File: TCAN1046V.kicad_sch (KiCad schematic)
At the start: 5 parts, among them U2 TCAN1051VDRBRQ1

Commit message: OBC: Continue PCB lauout
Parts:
- removed U2: TCAN1051VDRBRQ1, TCAN1051V:DRB8_TEX, symbol TCAN1051V:TCAN1051VDRBRQ1
- added U3: TCAN1046AVDYYRQ1, TCAN1046AV:SOT23_DYY_TEX, symbol TCAN1046AVDYYRQ1:TCAN1046AVDYYRQ1
- renumbered C3 to C4, C4 to C5, C5 to C6, C6 to C7
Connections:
- net GND: now also U3.2 (GND1), U3.5 (GND2)
- net VCC: now also U3.3 (VCC)
- net VIO: now also U3.11 (VIO)
- new net CANH1: U3.13 (CANH1)
- new net CANH2: U3.10 (CANH2)
- new net CANL1: U3.12 (CANL1)
- new net CANL2: U3.9 (CANL2)
- new net RXD1: U3.4 (RXD1)
- new net RXD2: U3.7 (RXD2)
- new net STB1: U3.14 (STB1)
- new net STB2: U3.8 (STB2/NSTB2)
- new net TXD1: U3.1 (TXD1)
- new net TXD2: U3.6 (TXD2)
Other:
- moved on the sheet: C4, C5, C6, C7

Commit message: Layout confirmed, PCBs ordered
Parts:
- C4, C6: DigiKey Part Number (none) -> 720-GA0805Y472KXBBC31GCT-ND
- C5, C7: DigiKey Part Number (none) -> 720-GA0805Y104JXABT31GCT-ND
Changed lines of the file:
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@@
 			)
 		)
-		(property "Datasheet" "https://www.ti.com/lit/gpn/tcan1046av-q1"
+		(property "Datasheet" ""
 			(at 186.69 128.27 0)
 			(effects
@@
 			)
 		)
+		(property "DigiKey Part Number" "720-GA0805Y104JXABT31GCT-ND"
+			(at 259.08 139.7 0)
+			(effects
+				(font
+					(size 1.27 1.27)
+				)
+				(hide yes)
+			)
+		)
 		(pin "2"
 		)
@@
 			)
 		)
+		(property "DigiKey Part Number" "720-GA0805Y472KXBBC31GCT-ND"
+			(at 250.19 139.7 0)
+			(effects
+				(font
+					(size 1.27 1.27)
+				)
+				(hide yes)
+			)
+		)
 		(pin "2"
 		)
@@
 			)
 		)
+		(property "DigiKey Part Number" "720-GA0805Y472KXBBC31GCT-ND"
+			(at 161.29 142.24 0)
+			(effects
+				(font
+					(size 1.27 1.27)
+				)
+				(hide yes)
+			)
+		)
 		(pin "2"
 		)
@@
 			(at 170.18 142.24 0)
 			(effects
+				(font
+					(size 1.27 1.27)
+				)
+				(hide yes)
+			)
+		)
+		(property "DigiKey Part Number" "720-GA0805Y104JXABT31GCT-ND"
+			(at 170.18 142.24 0)
+			(effects

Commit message: Separate PCBs into individual repos to allow for multiple workgroups
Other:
- title: HEDGE2 Avionics -> HEDGE2 OBC
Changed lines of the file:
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@@
 	(paper "USLedger")
 	(title_block
-		(title "HEDGE2 Avionics")
+		(title "HEDGE2 OBC")
 		(date "2025-06-27")
 		(rev "V0.8")
@@
 		)
 		(instances
-			(project "Avionics"
+			(project "HEDGE2-OBC"
 				(path "/ace5002f-3cbc-4a0a-869b-0e31ebd905b7/893aef5a-59ff-410b-9a71-9930aaf04e9f/d3868309-a946-47d2-bb65-3f159979e5fb"
 					(reference "U3")
@@
 		)
 		(instances
-			(project "Avionics"
+			(project "HEDGE2-OBC"
 				(path "/ace5002f-3cbc-4a0a-869b-0e31ebd905b7/893aef5a-59ff-410b-9a71-9930aaf04e9f/d3868309-a946-47d2-bb65-3f159979e5fb"
 					(reference "#PWR068")
@@
 		)
 		(instances
-			(project "Avionics"
+			(project "HEDGE2-OBC"
 				(path "/ace5002f-3cbc-4a0a-869b-0e31ebd905b7/893aef5a-59ff-410b-9a71-9930aaf04e9f/d3868309-a946-47d2-bb65-3f159979e5fb"
 					(reference "C7")
@@
 		)
 		(instances
-			(project "Avionics"
+			(project "HEDGE2-OBC"
 				(path "/ace5002f-3cbc-4a0a-869b-0e31ebd905b7/893aef5a-59ff-410b-9a71-9930aaf04e9f/d3868309-a946-47d2-bb65-3f159979e5fb"
 					(reference "C6")
@@
 		)
 		(instances
-			(project "Avionics"
+			(project "HEDGE2-OBC"
 				(path "/ace5002f-3cbc-4a0a-869b-0e31ebd905b7/893aef5a-59ff-410b-9a71-9930aaf04e9f/d3868309-a946-47d2-bb65-3f159979e5fb"
 					(reference "#PWR067")
@@
 		)
 		(instances
-			(project "Avionics"
+			(project "HEDGE2-OBC"
 				(path "/ace5002f-3cbc-4a0a-869b-0e31ebd905b7/893aef5a-59ff-410b-9a71-9930aaf04e9f/d3868309-a946-47d2-bb65-3f159979e5fb"
 					(reference "#PWR069")
@@
 		)
 		(instances
-			(project "Avionics"
+			(project "HEDGE2-OBC"
 				(path "/ace5002f-3cbc-4a0a-869b-0e31ebd905b7/893aef5a-59ff-410b-9a71-9930aaf04e9f/d3868309-a946-47d2-bb65-3f159979e5fb"
 					(reference "C4")
@@
 		)
 		(instances
-			(project "Avionics"
+			(project "HEDGE2-OBC"
 				(path "/ace5002f-3cbc-4a0a-869b-0e31ebd905b7/893aef5a-59ff-410b-9a71-9930aaf04e9f/d3868309-a946-47d2-bb65-3f159979e5fb"
 					(reference "C5")
@@
 		)
 		(instances
-			(project "Avionics"
+			(project "HEDGE2-OBC"
 				(path "/ace5002f-3cbc-4a0a-869b-0e31ebd905b7/893aef5a-59ff-410b-9a71-9930aaf04e9f/d3868309-a946-47d2-bb65-3f159979e5fb"
 					(reference "#PWR070")

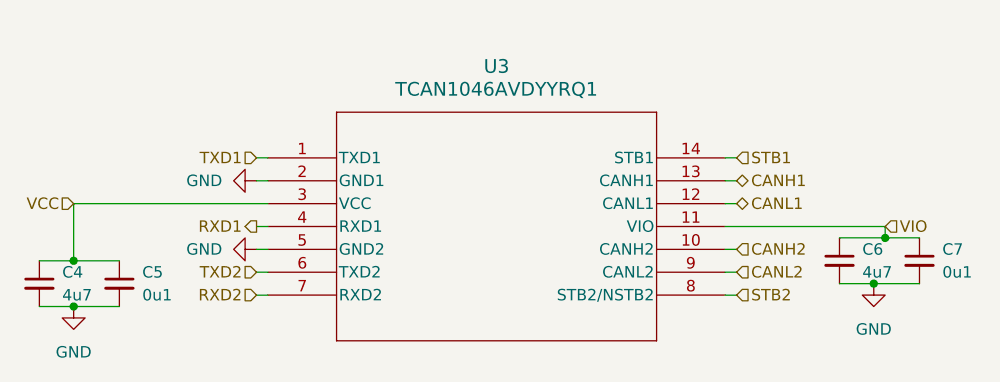
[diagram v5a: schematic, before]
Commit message: Cleanup after splitting PCBs into separate repos
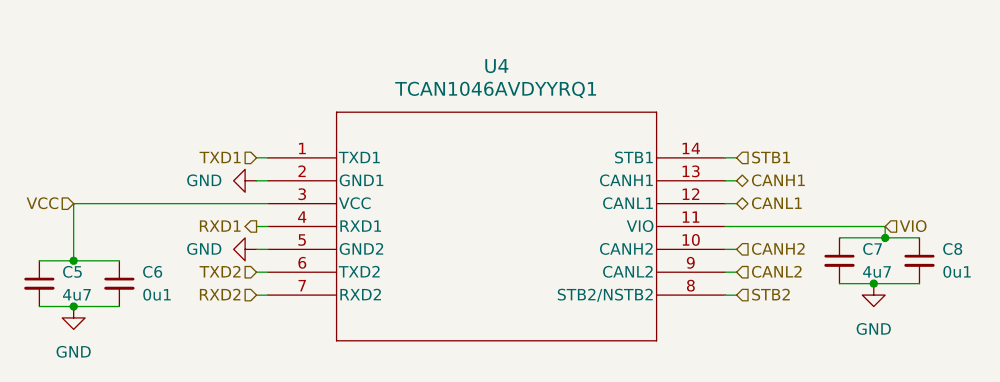
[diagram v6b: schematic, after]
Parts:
- renumbered C4 to C5, C5 to C6, C6 to C7, C7 to C8, U3 to U4
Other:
- title: HEDGE2 OBC -> HEDGE-2 OBC
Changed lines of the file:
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@@
 	(paper "USLedger")
 	(title_block
-		(title "HEDGE2 OBC")
-		(date "2025-06-27")
-		(rev "V0.8")
+		(title "HEDGE-2 OBC")
+		(date "2025-09-08")
+		(rev "V1.0")
 		(company "University of Virginia")
 		(comment 1 "Department of Mechanical and Aerospace Engineering")
@@
 		(dnp no)
 		(fields_autoplaced yes)
-		(property "Reference" "U3"
+		(property "Reference" "U4"
 			(at 212.09 118.11 0)
 			(effects
@@
 		(instances
 			(project "HEDGE2-OBC"
-				(path "/ace5002f-3cbc-4a0a-869b-0e31ebd905b7/893aef5a-59ff-410b-9a71-9930aaf04e9f/d3868309-a946-47d2-bb65-3f159979e5fb"
-					(reference "U3")
+				(path "/a13a6ce3-91ba-42e3-9b40-443fe6a0f2d9/d3868309-a946-47d2-bb65-3f159979e5fb"
+					(reference "U4")
 					(unit 1)
 				)
@@
 		(dnp no)
 		(fields_autoplaced yes)
-		(property "Reference" "#PWR068"
+		(property "Reference" "#PWR051"
 			(at 179.07 130.81 0)
 			(effects
@@
 		(instances
 			(project "HEDGE2-OBC"
-				(path "/ace5002f-3cbc-4a0a-869b-0e31ebd905b7/893aef5a-59ff-410b-9a71-9930aaf04e9f/d3868309-a946-47d2-bb65-3f159979e5fb"
-					(reference "#PWR068")
+				(path "/a13a6ce3-91ba-42e3-9b40-443fe6a0f2d9/d3868309-a946-47d2-bb65-3f159979e5fb"
+					(reference "#PWR051")
 					(unit 1)
 				)
@@
 		(dnp no)
 		(fields_autoplaced yes)
-		(property "Reference" "C7"
+		(property "Reference" "C8"
 			(at 261.62 138.4362 0)
 			(effects
@@
 		(instances
 			(project "HEDGE2-OBC"
-				(path "/ace5002f-3cbc-4a0a-869b-0e31ebd905b7/893aef5a-59ff-410b-9a71-9930aaf04e9f/d3868309-a946-47d2-bb65-3f159979e5fb"
-					(reference "C7")
+				(path "/a13a6ce3-91ba-42e3-9b40-443fe6a0f2d9/d3868309-a946-47d2-bb65-3f159979e5fb"
+					(reference "C8")
 					(unit 1)
 				)
@@
 		(dnp no)
 		(fields_autoplaced yes)
-		(property "Reference" "C6"
+		(property "Reference" "C7"
 			(at 252.73 138.4362 0)
 			(effects
@@
 		(instances
 			(project "HEDGE2-OBC"
-				(path "/ace5002f-3cbc-4a0a-869b-0e31ebd905b7/893aef5a-59ff-410b-9a71-9930aaf04e9f/d3868309-a946-47d2-bb65-3f159979e5fb"
-					(reference "C6")
+				(path "/a13a6ce3-91ba-42e3-9b40-443fe6a0f2d9/d3868309-a946-47d2-bb65-3f159979e5fb"
+					(reference "C7")
 					(unit 1)
 				)
@@
 		(dnp no)
 		(fields_autoplaced yes)
-		(property "Reference" "#PWR067"
+		(property "Reference" "#PWR050"
 			(at 165.1 151.13 0)
 			(effects
@@
 		(instances
 			(project "HEDGE2-OBC"
-				(path "/ace5002f-3cbc-4a0a-869b-0e31ebd905b7/893aef5a-59ff-410b-9a71-9930aaf04e9f/d3868309-a946-47d2-bb65-3f159979e5fb"
-					(reference "#PWR067")
+				(path "/a13a6ce3-91ba-42e3-9b40-443fe6a0f2d9/d3868309-a946-47d2-bb65-3f159979e5fb"
+					(reference "#PWR050")
 					(unit 1)
 				)
@@
 		(dnp no)
 		(fields_autoplaced yes)
-		(property "Reference" "#PWR069"
+		(property "Reference" "#PWR052"
 			(at 179.07 138.43 0)
 			(effects
@@
 		(instances
 			(project "HEDGE2-OBC"
-				(path "/ace5002f-3cbc-4a0a-869b-0e31ebd905b7/893aef5a-59ff-410b-9a71-9930aaf04e9f/d3868309-a946-47d2-bb65-3f159979e5fb"
-					(reference "#PWR069")
+				(path "/a13a6ce3-91ba-42e3-9b40-443fe6a0f2d9/d3868309-a946-47d2-bb65-3f159979e5fb"
+					(reference "#PWR052")
 					(unit 1)
 				)
@@
 		(dnp no)
 		(fields_autoplaced yes)
-		(property "Reference" "C4"
+		(property "Reference" "C5"
 			(at 163.83 140.9762 0)
 			(effects
@@
 		(instances
 			(project "HEDGE2-OBC"
-				(path "/ace5002f-3cbc-4a0a-869b-0e31ebd905b7/893aef5a-59ff-410b-9a71-9930aaf04e9f/d3868309-a946-47d2-bb65-3f159979e5fb"
-					(reference "C4")
+				(path "/a13a6ce3-91ba-42e3-9b40-443fe6a0f2d9/d3868309-a946-47d2-bb65-3f159979e5fb"
+					(reference "C5")
 					(unit 1)
 				)
@@
 		(dnp no)
 		(fields_autoplaced yes)
-		(property "Reference" "C5"
+		(property "Reference" "C6"
 			(at 172.72 140.9762 0)
 			(effects
@@
 		(instances
 			(project "HEDGE2-OBC"
-				(path "/ace5002f-3cbc-4a0a-869b-0e31ebd905b7/893aef5a-59ff-410b-9a71-9930aaf04e9f/d3868309-a946-47d2-bb65-3f159979e5fb"
-					(reference "C5")
+				(path "/a13a6ce3-91ba-42e3-9b40-443fe6a0f2d9/d3868309-a946-47d2-bb65-3f159979e5fb"
+					(reference "C6")
 					(unit 1)
 				)
@@
 		(dnp no)
 		(fields_autoplaced yes)
-		(property "Reference" "#PWR070"
+		(property "Reference" "#PWR053"
 			(at 254 148.59 0)
 			(effects
@@
 		(instances
 			(project "HEDGE2-OBC"
-				(path "/ace5002f-3cbc-4a0a-869b-0e31ebd905b7/893aef5a-59ff-410b-9a71-9930aaf04e9f/d3868309-a946-47d2-bb65-3f159979e5fb"
-					(reference "#PWR070")
+				(path "/a13a6ce3-91ba-42e3-9b40-443fe6a0f2d9/d3868309-a946-47d2-bb65-3f159979e5fb"
+					(reference "#PWR053")
 					(unit 1)
 				)

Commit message: Add RS-485 interfaces; modify for 5V power input
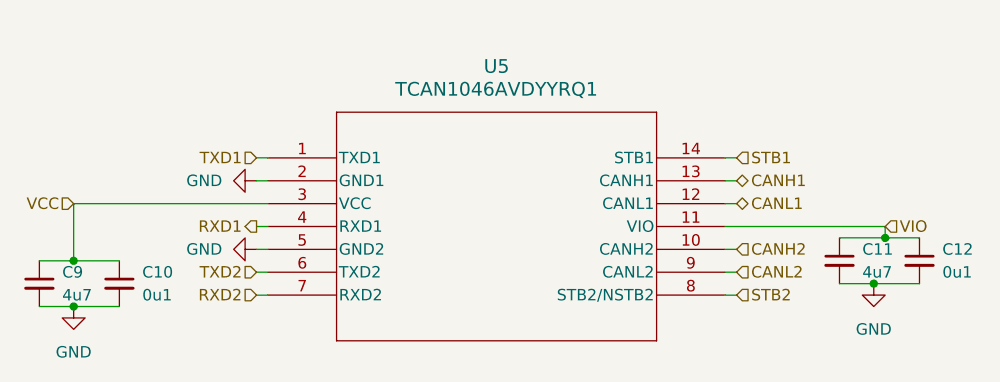
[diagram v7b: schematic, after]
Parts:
- renumbered C6 to C10, C7 to C11, C8 to C12, C5 to C9, U4 to U5
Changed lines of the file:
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@@
 		(dnp no)
 		(fields_autoplaced yes)
-		(property "Reference" "U4"
+		(property "Reference" "U5"
 			(at 212.09 118.11 0)
 			(effects
@@
 			(project "HEDGE2-OBC"
 				(path "/a13a6ce3-91ba-42e3-9b40-443fe6a0f2d9/d3868309-a946-47d2-bb65-3f159979e5fb"
-					(reference "U4")
+					(reference "U5")
 					(unit 1)
 				)
@@
 		(dnp no)
 		(fields_autoplaced yes)
-		(property "Reference" "#PWR051"
+		(property "Reference" "#PWR055"
 			(at 179.07 130.81 0)
 			(effects
@@
 			(project "HEDGE2-OBC"
 				(path "/a13a6ce3-91ba-42e3-9b40-443fe6a0f2d9/d3868309-a946-47d2-bb65-3f159979e5fb"
-					(reference "#PWR051")
+					(reference "#PWR055")
 					(unit 1)
 				)
@@
 		(dnp no)
 		(fields_autoplaced yes)
-		(property "Reference" "C8"
+		(property "Reference" "C12"
 			(at 261.62 138.4362 0)
 			(effects
@@
 			(project "HEDGE2-OBC"
 				(path "/a13a6ce3-91ba-42e3-9b40-443fe6a0f2d9/d3868309-a946-47d2-bb65-3f159979e5fb"
-					(reference "C8")
+					(reference "C12")
 					(unit 1)
 				)
@@
 		(dnp no)
 		(fields_autoplaced yes)
-		(property "Reference" "C7"
+		(property "Reference" "C11"
 			(at 252.73 138.4362 0)
 			(effects
@@
 			(project "HEDGE2-OBC"
 				(path "/a13a6ce3-91ba-42e3-9b40-443fe6a0f2d9/d3868309-a946-47d2-bb65-3f159979e5fb"
-					(reference "C7")
+					(reference "C11")
 					(unit 1)
 				)
@@
 		(dnp no)
 		(fields_autoplaced yes)
-		(property "Reference" "#PWR050"
+		(property "Reference" "#PWR054"
 			(at 165.1 151.13 0)
 			(effects
@@
 			(project "HEDGE2-OBC"
 				(path "/a13a6ce3-91ba-42e3-9b40-443fe6a0f2d9/d3868309-a946-47d2-bb65-3f159979e5fb"
-					(reference "#PWR050")
+					(reference "#PWR054")
 					(unit 1)
 				)
@@
 		(dnp no)
 		(fields_autoplaced yes)
-		(property "Reference" "#PWR052"
+		(property "Reference" "#PWR056"
 			(at 179.07 138.43 0)
 			(effects
@@
 			(project "HEDGE2-OBC"
 				(path "/a13a6ce3-91ba-42e3-9b40-443fe6a0f2d9/d3868309-a946-47d2-bb65-3f159979e5fb"
-					(reference "#PWR052")
+					(reference "#PWR056")
 					(unit 1)
 				)
@@
 		(dnp no)
 		(fields_autoplaced yes)
-		(property "Reference" "C5"
+		(property "Reference" "C9"
 			(at 163.83 140.9762 0)
 			(effects
@@
 			(project "HEDGE2-OBC"
 				(path "/a13a6ce3-91ba-42e3-9b40-443fe6a0f2d9/d3868309-a946-47d2-bb65-3f159979e5fb"
-					(reference "C5")
+					(reference "C9")
 					(unit 1)
 				)
@@
 		(dnp no)
 		(fields_autoplaced yes)
-		(property "Reference" "C6"
+		(property "Reference" "C10"
 			(at 172.72 140.9762 0)
 			(effects
@@
 			(project "HEDGE2-OBC"
 				(path "/a13a6ce3-91ba-42e3-9b40-443fe6a0f2d9/d3868309-a946-47d2-bb65-3f159979e5fb"
-					(reference "C6")
+					(reference "C10")
 					(unit 1)
 				)
@@
 		(dnp no)
 		(fields_autoplaced yes)
-		(property "Reference" "#PWR053"
+		(property "Reference" "#PWR057"
 			(at 254 148.59 0)
 			(effects
@@
 			(project "HEDGE2-OBC"
 				(path "/a13a6ce3-91ba-42e3-9b40-443fe6a0f2d9/d3868309-a946-47d2-bb65-3f159979e5fb"
-					(reference "#PWR053")
-					(unit 1)
-				)
+					(reference "#PWR057")
+					(unit 1)
+				)
